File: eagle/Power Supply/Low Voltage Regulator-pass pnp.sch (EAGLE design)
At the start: 5 parts, among them IC1 UA723N, P1 5k

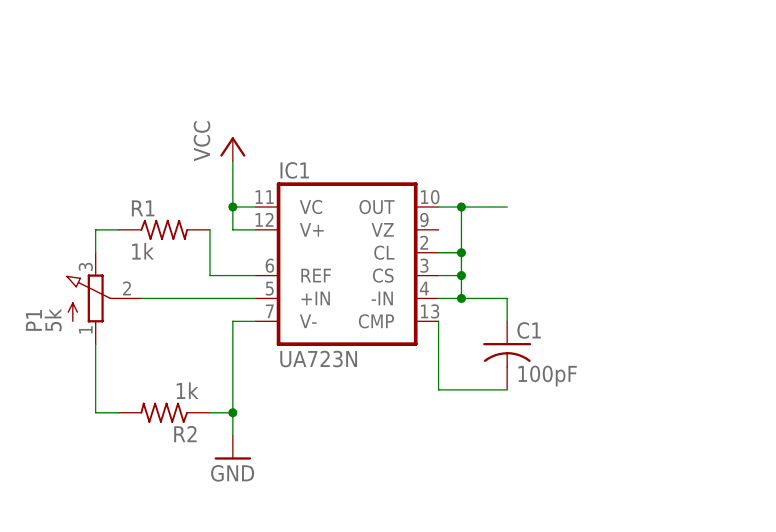
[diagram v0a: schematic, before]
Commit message: Low Voltage Regular schematics
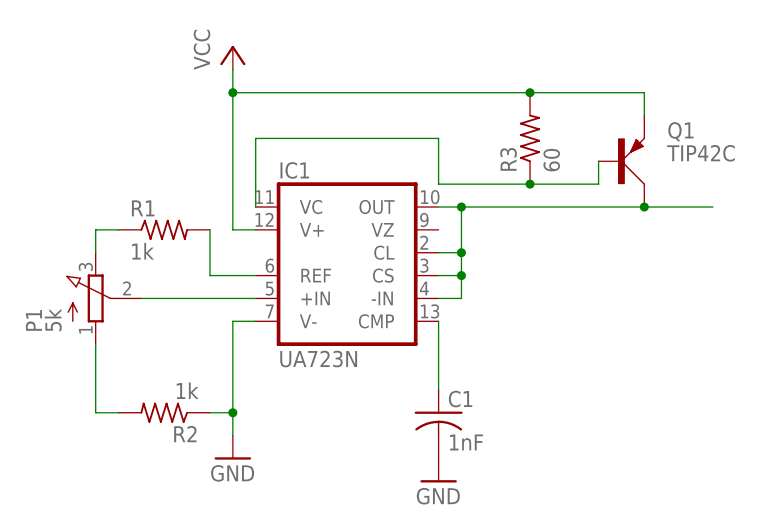
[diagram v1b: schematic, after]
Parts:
- added Q1: TIP42C, transistor-power:TIP42C
- added R3: 60, rcl:R-US_0207/10
- C1: value 100pF -> 1nF
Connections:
- new net N$7: IC1.VC, Q1.B, R3.1
- net GND: now also C1.2
- net N$4: now also C1.1; no longer C1.2
- net N$5: now also Q1.C; no longer C1.1
- net VCC: now also Q1.E, R3.2; no longer IC1.VC
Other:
- moved on the sheet: C1
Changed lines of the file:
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@@
 <part name="R1" library="rcl" deviceset="R-US_" device="0207/10" value="1k"/>
 <part name="R2" library="rcl" deviceset="R-US_" device="0207/10" value="1k"/>
-<part name="C1" library="rcl" deviceset="C-US" device="050-025X075" value="100pF"/>
+<part name="C1" library="rcl" deviceset="C-US" device="050-025X075" value="1nF"/>
 <part name="P1" library="pot" deviceset="3RP/1610N" device="" value="5k"/>
+<part name="Q1" library="transistor-power" deviceset="TIP42C" device=""/>
+<part name="R3" library="rcl" deviceset="R-US_" device="0207/10" value="60"/>
+<part name="GND2" library="supply1" deviceset="GND" device=""/>
 </parts>
 <sheets>
@@
 <instances>
 <instance part="IC1" gate="A" x="58.42" y="53.34"/>
-<instance part="P+1" gate="VCC" x="45.72" y="66.04"/>
+<instance part="P+1" gate="VCC" x="45.72" y="76.2"/>
 <instance part="GND1" gate="1" x="45.72" y="30.48"/>
 <instance part="R1" gate="G$1" x="38.1" y="55.88"/>
 <instance part="R2" gate="G$1" x="38.1" y="35.56" rot="R180"/>
-<instance part="C1" gate="G$1" x="76.2" y="43.18"/>
+<instance part="C1" gate="G$1" x="68.58" y="35.56"/>
 <instance part="P1" gate="G$1" x="30.48" y="48.26"/>
+<instance part="Q1" gate="1" x="88.9" y="63.5"/>
+<instance part="R3" gate="G$1" x="78.74" y="66.04" rot="R90"/>
+<instance part="GND2" gate="1" x="68.58" y="27.94"/>
 </instances>
 <busses>
@@
 <junction x="45.72" y="35.56"/>
 </segment>
+<segment>
+<pinref part="C1" gate="G$1" pin="2"/>
+<pinref part="GND2" gate="1" pin="GND"/>
+</segment>
 </net>
 <net name="VCC" class="0">
@@
 <pinref part="P+1" gate="VCC" pin="VCC"/>
 <wire x1="48.26" y1="55.88" x2="45.72" y2="55.88" width="0.1524" layer="91"/>
-<wire x1="45.72" y1="55.88" x2="45.72" y2="58.42" width="0.1524" layer="91"/>
-<pinref part="IC1" gate="A" pin="VC"/>
-<wire x1="45.72" y1="58.42" x2="45.72" y2="63.5" width="0.1524" layer="91"/>
-<wire x1="48.26" y1="58.42" x2="45.72" y2="58.42" width="0.1524" layer="91"/>
-<junction x="45.72" y="58.42"/>
+<wire x1="45.72" y1="55.88" x2="45.72" y2="71.12" width="0.1524" layer="91"/>
+<pinref part="Q1" gate="1" pin="E"/>
+<wire x1="45.72" y1="71.12" x2="45.72" y2="73.66" width="0.1524" layer="91"/>
+<wire x1="45.72" y1="71.12" x2="78.74" y2="71.12" width="0.1524" layer="91"/>
+<wire x1="78.74" y1="71.12" x2="91.44" y2="71.12" width="0.1524" layer="91"/>
+<wire x1="91.44" y1="71.12" x2="91.44" y2="68.58" width="0.1524" layer="91"/>
+<junction x="45.72" y="71.12"/>
+<pinref part="R3" gate="G$1" pin="2"/>
+<junction x="78.74" y="71.12"/>
 </segment>
 </net>
 <net name="N$4" class="0">
 <segment>
-<pinref part="C1" gate="G$1" pin="2"/>
 <pinref part="IC1" gate="A" pin="CMP"/>
-<wire x1="76.2" y1="38.1" x2="68.58" y2="38.1" width="0.1524" layer="91"/>
 <wire x1="68.58" y1="38.1" x2="68.58" y2="45.72" width="0.1524" layer="91"/>
+<pinref part="C1" gate="G$1" pin="1"/>
 </segment>
 </net>
@@
 <wire x1="68.58" y1="58.42" x2="71.12" y2="58.42" width="0.1524" layer="91"/>
 <pinref part="IC1" gate="A" pin="CL"/>
-<wire x1="71.12" y1="58.42" x2="76.2" y2="58.42" width="0.1524" layer="91"/>
 <wire x1="68.58" y1="53.34" x2="71.12" y2="53.34" width="0.1524" layer="91"/>
 <wire x1="71.12" y1="53.34" x2="71.12" y2="58.42" width="0.1524" layer="91"/>
@@
 <junction x="71.12" y="53.34"/>
 <pinref part="IC1" gate="A" pin="-IN"/>
-<pinref part="C1" gate="G$1" pin="1"/>
 <wire x1="68.58" y1="48.26" x2="71.12" y2="48.26" width="0.1524" layer="91"/>
-<wire x1="71.12" y1="48.26" x2="76.2" y2="48.26" width="0.1524" layer="91"/>
-<wire x1="76.2" y1="48.26" x2="76.2" y2="45.72" width="0.1524" layer="91"/>
 <wire x1="71.12" y1="50.8" x2="71.12" y2="48.26" width="0.1524" layer="91"/>
 <junction x="71.12" y="50.8"/>
-<junction x="71.12" y="48.26"/>
+<pinref part="Q1" gate="1" pin="C"/>
+<wire x1="71.12" y1="58.42" x2="91.44" y2="58.42" width="0.1524" layer="91"/>
+<wire x1="91.44" y1="58.42" x2="99.06" y2="58.42" width="0.1524" layer="91"/>
+<junction x="91.44" y="58.42"/>
 </segment>
 </net>
@@
 </segment>
 </net>
+<net name="N$7" class="0">
+<segment>
+<pinref part="Q1" gate="1" pin="B"/>
+<wire x1="86.36" y1="63.5" x2="86.36" y2="60.96" width="0.1524" layer="91"/>
+<pinref part="R3" gate="G$1" pin="1"/>
+<wire x1="86.36" y1="60.96" x2="78.74" y2="60.96" width="0.1524" layer="91"/>
+<wire x1="78.74" y1="60.96" x2="68.58" y2="60.96" width="0.1524" layer="91"/>
+<wire x1="68.58" y1="60.96" x2="68.58" y2="66.04" width="0.1524" layer="91"/>
+<junction x="78.74" y="60.96"/>
+<pinref part="IC1" gate="A" pin="VC"/>
+<wire x1="68.58" y1="66.04" x2="48.26" y2="66.04" width="0.1524" layer="91"/>
+<wire x1="48.26" y1="66.04" x2="48.26" y2="58.42" width="0.1524" layer="91"/>
+</segment>
+</net>
